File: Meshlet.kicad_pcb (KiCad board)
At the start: 2 copper layers, 60.2 x 39 mm, 114 parts, among them J1 Ext. Notif. Header, J10 STEMMA QT I2C, J11 GPIO Exp., J12 I2C PINHEADER, J13 Ext. Power Header, J2 USB_C_Receptacle_USB2.0_16P, J3 Ext. Power Header, J4 Batt. Header (JST-PH 2.0), J5 SWD, J6 Batt. Header (Picoblade 1.25), J7 GPS Header, J8 User Btn Header, J9 Power Switch, Q1 AO3400A, SW1 BOOTSEL, SW3 RST, U1 W25Q32JVZP, U10 XC6206PxxxMR, U11 XC6206PxxxMR, U2 XC6206PxxxMR, U3 RP2350_60QFN, U4 INA3221, U5 BME280, U6 Wio-SX1262, U7 USBLC6-2SC6, U8 BQ24074RGT, Y1 12.000MHz

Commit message: Redesign!
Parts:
- removed G***: LOGO, Graphics:HalftoneOverlay
- removed J10: STEMMA QT I2C, Connector_JST:JST_PH_S4B-PH-SM4-TB_1x04-1MP_P2.00mm_Horizontal
- removed J8: User Btn Header, Connector_PinHeader_1.27mm:PinHeader_1x02_P1.27mm_Vertical
- removed JP6: PwrSw Bypass, Jumper:SolderJumper-2_P1.3mm_Bridged_RoundedPad1.0x1.5mm
- removed R29, R30, R33, R34, R35: 10k, Resistor_SMD:R_0402_1005Metric
- removed R31: 1k, Resistor_SMD:R_0402_1005Metric
- removed R32: 470R, Resistor_SMD:R_0402_1005Metric
- removed REF** (x2): MountingHole_2.2mm_M2_Pad_TopBottom, MountingHole:MountingHole_2.2mm_M2_Pad_TopBottom
- removed REF** (x2): ToolingHole_1.152mm, MountingHole:ToolingHole_1.152mm
- removed SW3: RST, Button_Switch_SMD:SW_Push_1P1T_XKB_TS-1187A
- removed TH1: Thermistor_NTC, Resistor_SMD:R_0402_1005Metric_Pad0.72x0.64mm_HandSolder
- added C32: 47uF, Capacitor_SMD:C_0805_2012Metric, B.Cu at (135.9, 109.1)
- added J14: Ext. Notif. Header, Connector_PinHeader_2.00mm:PinHeader_1x02_P2.00mm_Vertical, F.Cu at (123.8, 97.9)
- added JP1: TS, Jumper:SolderJumper-2_P1.3mm_Bridged_RoundedPad1.0x1.5mm, F.Cu at (140.1, 106.8)
- added R5: 27R, Resistor_SMD:R_0402_1005Metric, F.Cu at (145.5, 87.5)
- added SW2: BOOTSEL, Button_Switch_SMD:SW_Push_1P1T_XKB_TS-1187A, F.Cu at (139.1, 96.7)
- C1: value 15pF -> 100nF
- C13, C18, C19: value 100nF -> 1uF
- C14: value 100nF -> 4.7uF
- C15, C17: value 100nF -> 4.7uF; footprint Capacitor_SMD:C_0402_1005Metric -> RP2350 Components:C_0402_1005Metric_small_pads
- C2: value 15pF -> 4.7uF
- C20: value 100nF -> 47uF; footprint Capacitor_SMD:C_0402_1005Metric -> Capacitor_SMD:C_0805_2012Metric
- C21: value 100nF -> 15pF
- C24: value 47uF -> 15pF; footprint Capacitor_SMD:C_0805_2012Metric -> Capacitor_SMD:C_0402_1005Metric
- C25, C9: value 1uF -> 100nF
- C26, C27, C28: value 1uF -> 22uF
- C29, C30: value 47uF -> 1uF; footprint Capacitor_SMD:C_0805_2012Metric -> Capacitor_SMD:C_0402_1005Metric
- C3, C5: value 4.7uF -> 100nF; footprint RP2350 Components:C_0402_1005Metric_small_pads -> Capacitor_SMD:C_0402_1005Metric
- C31: value 47uF -> 100nF; footprint Capacitor_SMD:C_0805_2012Metric -> Capacitor_SMD:C_0402_1005Metric
- C6, C7: value 4.7uF -> 100nF
- D3: value PG -> HB
- D4: value CHG -> PV
- D5: value PWR -> CHG
- D6: value HB -> FLT
- J1: value Ext. Notif. Header -> SWD; footprint Connector_PinHeader_1.27mm:PinHeader_1x02_P1.27mm_Vertical -> Connector_PinHeader_1.27mm:PinHeader_1x03_P1.27mm_Vertical; moved to B.Cu
- J11: footprint Connector_PinHeader_1.27mm:PinHeader_1x04_P1.27mm_Vertical -> Connector_PinHeader_2.00mm:PinHeader_1x05_P2.00mm_Vertical; moved to B.Cu
- J12: value I2C PINHEADER -> GPS Header; footprint Connector_PinHeader_1.27mm:PinHeader_1x04_P1.27mm_Vertical -> Connector_PinHeader_2.00mm:PinHeader_1x05_P2.00mm_Vertical; moved to B.Cu
- J13: value Ext. Power Header -> Thermistor Pins
- J2: value USB_C_Receptacle_USB2.0_16P -> User Btn Header; footprint Connector_USB:USB_C_Receptacle_G-Switch_GT-USB-7010ASV -> Connector_PinHeader_2.00mm:PinHeader_1x02_P2.00mm_Vertical
- J3: value Ext. Power Header -> Batt. Header (Picoblade 1.25); footprint Connector_JST:JST_XH_S2B-XH-A_1x02_P2.50mm_Horizontal -> Connector_Molex:Molex_PicoBlade_53261-0271_1x02-1MP_P1.25mm_Horizontal; moved to B.Cu
- J4: moved to B.Cu
- J5: value SWD -> USB_C_Receptacle_USB2.0_16P; footprint Connector_JST:JST_SH_SM03B-SRSS-TB_1x03-1MP_P1.00mm_Horizontal -> Connector_USB:USB_C_Receptacle_G-Switch_GT-USB-7010ASV
- J6: value Batt. Header (Picoblade 1.25) -> STEMMA QT I2C; footprint Connector_Molex:Molex_PicoBlade_53261-0271_1x02-1MP_P1.25mm_Horizontal -> Connector_PinHeader_2.00mm:PinHeader_1x04_P2.00mm_Vertical; moved to B.Cu
- J7: value GPS Header -> Ext. Power Header; footprint Connector_PinHeader_1.27mm:PinHeader_1x05_P1.27mm_Vertical -> Connector_JST:JST_PH_S2B-PH-SM4-TB_1x02-1MP_P2.00mm_Horizontal
- J9: value Power Switch -> Ext. Power Header; footprint Connector_PinHeader_2.00mm:PinHeader_1x02_P2.00mm_Vertical -> Connector_PinHeader_2.54mm:PinHeader_1x02_P2.54mm_Vertical; moved to B.Cu
- JP2: value ISET -> Chemistry Select; moved to B.Cu
- JP3: value EN1 -> SolderJumper_2_Open; footprint Jumper:SolderJumper-3_P1.3mm_Bridged12_RoundedPad1.0x1.5mm -> Jumper:SolderJumper-2_P1.3mm_Open_RoundedPad1.0x1.5mm
- JP4: value EN2 -> SolderJumper_2_Bridged; footprint Jumper:SolderJumper-3_P1.3mm_Bridged12_RoundedPad1.0x1.5mm -> Jumper:SolderJumper-2_P1.3mm_Bridged_RoundedPad1.0x1.5mm
- JP5: value Jumper_3_Bridged12 -> SolderJumper_2_Open; footprint Jumper:SolderJumper-3_P1.3mm_Bridged12_RoundedPad1.0x1.5mm -> Jumper:SolderJumper-2_P1.3mm_Open_RoundedPad1.0x1.5mm
- R10, R9: value 27R -> 1k
- R16: value 10k -> 13k
- R17: value 10k -> 1k
- R18: value 4.7k -> 5.1k
- R19: value 5.1k -> 300
- R2: value 1k -> 5.1k
- R20: value 5.1k -> 600
- R21: value 4.7k -> 1.2k
- R23, R26: value 1k -> PA2512FKF7W0R01E; footprint Resistor_SMD:R_0402_1005Metric -> Resistor_SMD:R_2512_6332Metric
- R24: value 10k -> PA2512FKF7W0R01E; footprint Resistor_SMD:R_0402_1005Metric -> Resistor_SMD:R_2512_6332Metric
- R25: value 10k -> 470R
- R27: value 1k -> 10k
- R3: value 0 -> 5.1k
- R4: value 1k -> 27R
- R6, R7, R8: value PA2512FKF7W0R01E -> 10k; footprint Resistor_SMD:R_2512_6332Metric -> Resistor_SMD:R_0402_1005Metric
- SW1: value BOOTSEL -> RST
- U1: value W25Q32JVZP -> XC6206PxxxMR; footprint Package_SON:WSON-8-1EP_6x5mm_P1.27mm_EP3.4x4.3mm -> Package_TO_SOT_SMD:SOT-23-3
- U10: value XC6206PxxxMR -> ~; footprint Package_TO_SOT_SMD:SOT-23-3 -> RM2:Radio Module 2; moved to B.Cu
- U11: value XC6206PxxxMR -> INA3221; footprint Package_TO_SOT_SMD:SOT-23-3 -> Package_DFN_QFN:Texas_RGV0016A_VQFN-16-1EP_4x4mm_P0.65mm_EP2.1x2.1mm
- U2: value XC6206PxxxMR -> USBLC6-2SC6; footprint Package_TO_SOT_SMD:SOT-23-3 -> Package_TO_SOT_SMD:SOT-23-6
- U3: value RP2350_60QFN -> XC6206PxxxMR; footprint RP2350_60QFN_minimal:RP2350-QFN-60-1EP_7x7_P0.4mm_EP3.4x3.4mm_ThermalVias -> Package_TO_SOT_SMD:SOT-23-3
- U4: value INA3221 -> RP2350_60QFN; footprint Package_DFN_QFN:Texas_RGV0016A_VQFN-16-1EP_4x4mm_P0.65mm_EP2.1x2.1mm -> RP2350_60QFN_minimal:RP2350-QFN-60-1EP_7x7_P0.4mm_EP3.4x3.4mm_ThermalVias
- U5: value BME280 -> Wio-SX1262; footprint Package_LGA:Bosch_LGA-8_2.5x2.5mm_P0.65mm_ClockwisePinNumbering -> Wio-SX1262:Wio-SX1262; moved to B.Cu
- U6: value Wio-SX1262 -> BQ25185; footprint Wio-SX1262:Wio-SX1262 -> Package_DFN_QFN:Texas_DLH0010A_WSON-10-1EP_2.2x2mm_P0.4mm_EP0.9x1.5mm_ThermalVias
- U7: value USBLC6-2SC6 -> BME280; footprint Package_TO_SOT_SMD:SOT-23-6 -> Package_LGA:Bosch_LGA-8_2.5x2.5mm_P0.65mm_ClockwisePinNumbering
- U8: value BQ24074RGT -> W25Q32JVZP; footprint Package_DFN_QFN:VQFN-16-1EP_3x3mm_P0.5mm_EP1.6x1.6mm -> Package_SON:WSON-8-1EP_6x5mm_P1.27mm_EP3.4x4.3mm
- U9: value ~ -> XC6206PxxxMR; footprint RM2:Radio Module 2 -> Package_TO_SOT_SMD:SOT-23-3; moved to F.Cu
- moved J7 58.9 mm to (160.2, 97.9)
- moved U9 57.4 mm to (134.1, 102.6)
- moved J5 49.3 mm to (161.2, 87.7), turned to 90 degrees
- moved F3 47.7 mm to (131.7, 103.0)
- moved J13 47.0 mm to (142.4, 103.3), turned to 90 degrees
- moved R21 46.7 mm to (132.6, 108.9), turned to 180 degrees
- moved R19 45.3 mm to (137.6, 108.9), turned to 180 degrees
- moved R20 44.8 mm to (135.1, 108.9), turned to 180 degrees
- moved C27 44.5 mm to (154.2, 106.6)
- moved C28 43.9 mm to (150.7, 107.9), turned to 180 degrees
- moved U6 43.0 mm to (153.3, 108.3), turned to 0 degrees
- moved U5 42.3 mm to (122.8, 80.3), turned to 0 degrees
- moved R2 41.3 mm to (157.2, 81.0), turned to 180 degrees
- moved R3 40.8 mm to (157.2, 82.0), turned to 0 degrees
- moved SW1 39.9 mm to (131.6, 96.7), turned to 0 degrees
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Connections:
- C1 pad 1: GND -> +1V1
- C1 pad 2: XIN -> GND
- C12 pad 1: /Pi +3V3 -> Net-(U1-VI)
- C13 pad 1: /Pi +3V3 -> +3V3
- C14 pad 1: /Pi +3V3 -> Net-(U4-VREG_AVDD)
- C16 pad 1: /Pi +3V3 -> USB_RAW
- C17 pad 1: GND -> +1V1
- C17 pad 2: +3V3 -> GND
- C18 pad 1: /Pi +3V3 -> Net-(U3-VI)
- C19 pad 1: /Pi +3V3 -> /LoRa +3V3
- C2 pad 1: GND -> +1V1
- C2 pad 2: Net-(C2-Pad2) -> GND
- C20 pad 1: /Pi +3V3 -> GND
- C20 pad 2: GND -> /LoRa +3V3
- C21 pad 1: +3V3 -> GND
- C21 pad 2: GND -> XIN
- C23 pad 1: INA_IN3- -> +3V3
- C24 pad 2: BMS_OUT -> Net-(C24-Pad2)
- C25 pad 1: Net-(U10-VI) -> /Pi +3V3
- C26 pad 1: /LoRa +3V3 -> BMS_INA
- C27 pad 1: Net-(U11-VI) -> VBUS_OUT
- C28 pad 1: +3V3 -> BATT
- C29 pad 1: BMS_OUT -> Net-(U9-VI)
- C3 pad 1: /Pi +3V3 -> +1V1
- C30 pad 1: INA_IN1+ -> /Pi +3V3
- C31 pad 2: /LoRa +3V3 -> +3V3
- C4 pad 1: +1V1 -> /Pi +3V3
- C5 pad 1: +1V1 -> /Pi +3V3
- C6 pad 1: Net-(U3-VREG_AVDD) -> /Pi +3V3
- C7 pad 1: +1V1 -> /Pi +3V3
- C8 pad 1: +1V1 -> /Pi +3V3
- C9 pad 1: Net-(U2-VI) -> /Pi +3V3
- D1 pad 1: VBUS -> VBUS_INA
- D1 pad 2: INA_IN3+ -> USB_RAW
- D2 pad 1: VBUS -> VBUS_INA
- D2 pad 2: INA_IN2+ -> Net-(D2-A)
- D3 pad 1: Net-(D3-K) -> GND
- D3 pad 2: BMS_OUT -> Net-(D3-A)
- D6 pad 1: GND -> Net-(D6-K)
- D6 pad 2: Net-(D6-A) -> BMS_OUT
- F1 pad 2: Net-(U2-VI) -> Net-(U1-VI)
- F2 pad 2: Net-(U10-VI) -> Net-(U3-VI)
- F3 pad 2: Net-(U11-VI) -> Net-(U9-VI)
- J1 pad 1: +3V3 -> SWCLK
- J1 pad 2: Net-(J1-Pin_2) -> GND
- J11 pad 1: +3V3 -> GP4
- J11 pad 2: INA_IN3- -> GP16
- J11 pad 3: BMS_OUT -> GP18
- J11 pad 4: GND -> GP19
- J12 pad 3: I2C_SCL -> GPS_TX
- J12 pad 4: I2C_SDA -> GPS_RX
- J13 pad 1: GND -> THERM
- J13 pad 2: INA_IN2- -> GND
- J3 pad 2: INA_IN2- -> BATT_INA
- J4 pad 2: INA_IN1- -> BATT_INA
- J6 pad 1: INA_IN1- -> I2C_SDA
- J6 pad 2: GND -> I2C_SCL
- J7 pad 2: +3V3 -> Net-(D2-A)
- J9 pad 1: Net-(J9-Pin_1) -> GND
- J9 pad 2: BMS_OUT -> Net-(D2-A)
- JP3 pad 1: BMS_OUT -> Net-(JP3-A)
- JP3 pad 2: BMS_EN1 -> ISET
- JP4 pad 1: GND -> Net-(JP4-A)
- JP4 pad 2: BMS_EN2 -> ISET
- JP5 pad 2: Net-(JP5-C) -> ISET
- L1 pad 2: Net-(U3-VREG_LX) -> Net-(U4-VREG_LX)
- Q1 pad 3: Net-(J1-Pin_2) -> Net-(J14-Pin_2)
- R1 pad 2: Net-(U3-VREG_AVDD) -> Net-(U4-VREG_AVDD)
- R10 pad 1: USB_DN -> Net-(R10-Pad1)
- R10 pad 2: Net-(U3-USB_DM) -> QSPI_SS
- R11 pad 1: INA_VPU -> Net-(U6-STAT1)
- R11 pad 2: INA_PV -> Net-(D6-K)
- R12 pad 1: +3V3 -> Net-(U6-STAT2)
- R12 pad 2: INA_CRIT -> Net-(D5-K)
- R13 pad 1: +3V3 -> GND
- R13 pad 2: INA_WARN -> Net-(U6-CE)
- R14 pad 1: +3V3 -> Net-(JP1-B)
- R14 pad 2: INA_TC -> GND
- R15 pad 1: +3V3 -> Net-(D4-K)
- R15 pad 2: I2C_SCL -> GND
- R16 pad 1: +3V3 -> VSET
- R16 pad 2: I2C_SDA -> Net-(JP2-B)
- R17 pad 1: NOTIFY -> Net-(C24-Pad2)
- R17 pad 2: Net-(Q1-G) -> XOUT
- R18 pad 1: I2C_SDA -> Net-(JP2-A)
- R18 pad 2: +3V3 -> VSET
- R19 pad 1: Net-(J2-CC1) -> GND
- R19 pad 2: GND -> Net-(JP3-A)
- R2 pad 1: Net-(R2-Pad1) -> Net-(J5-CC1)
- R2 pad 2: QSPI_SS -> GND
- R20 pad 2: Net-(J2-CC2) -> Net-(JP4-A)
- R21 pad 1: I2C_SCL -> GND
- R21 pad 2: +3V3 -> Net-(JP5-A)
- R22 pad 1: Net-(U8-ISET) -> INA_VPU
- R22 pad 2: Net-(JP2-A) -> INA_PV
- R23 pad 1: Net-(U8-ISET) -> BATT
- R23 pad 2: Net-(JP2-B) -> BATT_INA
- R24 pad 1: GND -> VBUS_INA
- R24 pad 2: Net-(U8-ITERM) -> VBUS_OUT
- R25 pad 1: Net-(U8-~{CE}) -> GP24
- R25 pad 2: GND -> Net-(U10-DO)
- R26 pad 1: GND -> BMS_INA
- R26 pad 2: Net-(U8-ILIM) -> BMS_OUT
- R27 pad 1: USER_BTN -> NOTIFY
- R27 pad 2: GND -> Net-(Q1-G)
- R28 pad 1: Net-(U8-~{PGOOD}) -> GP24
- R28 pad 2: Net-(D3-K) -> Net-(U10-IRQ)
- R3 pad 1: Net-(U1-~{CS}) -> GND
- R3 pad 2: QSPI_SS -> Net-(J5-CC2)
- R4 pad 1: Net-(C2-Pad2) -> USB_DP
- R4 pad 2: XOUT -> Net-(U4-USB_DP)
- R6 pad 1: INA_IN1+ -> +3V3
- R6 pad 2: INA_IN1- -> I2C_SCL
- R7 pad 1: INA_IN2+ -> +3V3
- R7 pad 2: INA_IN2- -> I2C_SDA
- R8 pad 1: INA_IN3+ -> Net-(D3-A)
- R8 pad 2: INA_IN3- -> Net-(U4-GPIO14)
- R9 pad 1: USB_DP -> Net-(R9-Pad1)
- R9 pad 2: Net-(U3-USB_DP) -> GND
- SW1 pad 1: Net-(R2-Pad1) -> Net-(U4-RUN)
- SW1 pad 2: GND -> Net-(R9-Pad1)
- U1 pad 1: Net-(U1-~{CS}) -> GND
- U1 pad 2: QSPI_SD1 -> +3V3
- U1 pad 3: QSPI_SD2 -> Net-(U1-VI)
- U10 pad 2: /LoRa +3V3 -> unconnected-(U10-NC-Pad2)
- U10 pad 3: Net-(U10-VI) -> GP29
- U11 pad 1: GND -> BMS_OUT
- U11 pad 2: +3V3 -> BMS_INA
- U11 pad 3: Net-(U11-VI) -> GND
- U2 pad 1: GND -> USB_DP
- U2 pad 2: /Pi +3V3 -> GND
- U2 pad 3: Net-(U2-VI) -> USB_DN
- U3 pad 1: /Pi +3V3 -> GND
- U3 pad 2: GPS_RX -> /LoRa +3V3
- U3 pad 3: GPS_TX -> Net-(U3-VI)
- U4 pad 1: INA_IN3- -> /Pi +3V3
- U4 pad 10: INA_PV -> unconnected-(U4-GPIO7-Pad10)
- U4 pad 11: INA_IN1- -> /Pi +3V3
- U4 pad 12: INA_IN1+ -> I2C_SDA
- U4 pad 13: INA_TC -> I2C_SCL
- U4 pad 14: INA_IN2- -> LORA_SCK
- U4 pad 15: INA_IN2+ -> LORA_MOSI
- U4 pad 16: INA_VPU -> LORA_MISO
- U4 pad 17: GND -> LORA_RF_SW
- U4 pad 2: INA_IN3+ -> GPS_RX
- U4 pad 3: GND -> GPS_TX
- U4 pad 4: +3V3 -> LORA_BUSY
- U4 pad 5: I2C_SDA -> LORA_CS
- U4 pad 6: I2C_SCL -> +1V1
- U4 pad 7: I2C_SDA -> GPS_EN
- U4 pad 8: INA_WARN -> GP4
- U4 pad 9: INA_CRIT -> unconnected-(U4-GPIO6-Pad9)
- U5 pad 1: GND -> LORA_RF_SW
- U5 pad 2: +3V3 -> LORA_MISO
- U5 pad 3: I2C_SDA -> LORA_MOSI
- U5 pad 4: I2C_SCL -> LORA_SCK
- U5 pad 5: GND -> LORA_RST
- U5 pad 6: +3V3 -> LORA_CS
- U5 pad 8: +3V3 -> /LoRa +3V3
- U6 pad 1: LORA_RF_SW -> BMS_INA
- U6 pad 10: GND -> VBUS_OUT
- U6 pad 11: LORA_BUSY -> GND
- U6 pad 2: LORA_MISO -> BATT
- U6 pad 3: LORA_MOSI -> Net-(U6-STAT2)
- U6 pad 4: LORA_SCK -> Net-(U6-CE)
- U6 pad 5: LORA_RST -> GND
- U6 pad 6: LORA_CS -> THERM
- U6 pad 7: GND -> VSET
- U6 pad 8: /LoRa +3V3 -> ISET
- U6 pad 9: unconnected-(U6-ANT-Pad9) -> Net-(U6-STAT1)
- U7 pad 1: USB_DP -> GND
- U7 pad 2: GND -> +3V3
- U7 pad 3: USB_DN -> I2C_SDA
- U7 pad 4: USB D- -> I2C_SCL
- U7 pad 5: INA_IN3- -> GND
- U7 pad 6: USB D+ -> +3V3
- U8 pad 1: Net-(JP5-C) -> QSPI_SS
- U8 pad 2: INA_IN1+ -> QSPI_SD1
- U8 pad 3: INA_IN1+ -> QSPI_SD2
- U8 pad 4: Net-(U8-~{CE}) -> GND
- U8 pad 5: BMS_EN2 -> QSPI_SD0
- U8 pad 6: BMS_EN1 -> QSPI_SCLK
- U8 pad 7: Net-(U8-~{PGOOD}) -> QSPI_SD3
- U8 pad 8: GND -> /Pi +3V3
- U8 pad 9: Net-(U8-~{CHG}) -> GND
- U9 pad 2: unconnected-(U9-NC-Pad2) -> /Pi +3V3
- U9 pad 3: GP29 -> Net-(U9-VI)
- Y1 pad 3: Net-(C2-Pad2) -> Net-(C24-Pad2)
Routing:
- net +3V3: track 155.0 -> 76.2 mm
- net I2C_SCL: track 110.2 -> 41.2 mm
- net I2C_SDA: track 109.1 -> 43.3 mm
- net BMS_OUT: track 110.8 -> 51.2 mm, vias 2 -> 4
- net INA_IN3-: track 48.5 -> 0.00 mm, vias 4 -> 0
- net GP29: track 48.1 -> 0.00 mm, vias 1 -> 0
- net GND: track 49.4 -> 1.75 mm, vias 323 -> 4
- net /Pi +3V3: track 99.3 -> 53.8 mm, vias 4 -> 3
- net Net-(U3-RUN): track 44.2 -> 0.00 mm, vias 2 -> 0
- net INA_IN1+: track 40.8 -> 0.00 mm, vias 2 -> 0
- net INA_IN1-: track 35.4 -> 0.00 mm
- net USB_RAW: track 0.00 -> 34.9 mm, vias 0 -> 2
- net INA_IN2-: track 31.4 -> 0.00 mm
- net GP25: track 42.9 -> 11.8 mm
- net Net-(D2-A): track 0.00 -> 30.9 mm, vias 0 -> 2
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- added copper zone on F.Cu, net BATT
- added copper zone on F.Cu, net BMS_INA
- added copper zone on In1.Cu, net GND
- added copper zone on In2.Cu, net GND
- added copper zone on F.Cu, net Net-(U4-VREG_LX)
- added copper zone on F.Cu, net VBUS_OUT
- removed copper zone on F.Cu, net Net-(U3-VREG_LX)
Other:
- board size 60.2 x 39 mm -> 42.5 x 32 mm
- copper layers 2 -> 4
- board text removed: "!"
- board text removed: "*4V4 MAX"
- board text removed: "*BMS"
- board text removed: "+"
- board text removed: "-"
- board text removed: "0"
- board text removed: "0.5A"
- board text removed: "1"
- board text removed: "1 SERIES CELL ONLY!"
- board text removed: "1A"
- board text removed: "3V"
- board text removed: "3V3"
- board text removed: "5V-10V"
- board text removed: ":"
- board text removed: "BOOT"
- board text removed: "Charge Rate (default 0.5A, 1A jumped)"
- board text removed: "DESIGNED IN"
- board text removed: "EDMONTON, AB"
- board text removed: "EN"
- board text removed: "EN1"
- board text removed: "EN1 (see datasheet, default high)"
- board text removed: "EN2"
- board text removed: "EN2 (see datasheet, default low)"
- board text removed: "EP V0.2"
- board text removed: "EXT. DC, SOLAR"
- board text removed: "EXTERNAL NOTIFS"
- board text removed: "GND"
- board text removed: "GP0"
- board text removed: "GP1"
- board text removed: "GP22"
- board text removed: "GP5"
- board text removed: "GPS"
- board text removed: "HEY!"
- board text removed: "I HOPE YOU HAVE A LONG ENOUGH USB CABLE"
- board text removed: "I2C"
- board text removed: "ISET"
- board text removed: "JP1:"
- board text removed: "JP2:"
- board text removed: "JP3:"
- board text removed: "JP4:"
- board text removed: "JP5:"
- board text removed: "JUMPER FUNCTIONS"
- board text removed: "LITHIUM ION & POLYMER"
- board text removed: "M2"
- board text removed: "MESH NETWORK NODE RP2350 MESH NETWORK NODE RP2350"
- board text removed: "MESHLET"
- board text removed: "MULTIPLE CELLS IN PARALLEL ARE OK IF YOU KNOW WHAT YOU'RE DOING"
- board text removed: "NOTIF."
- board text removed: "ON REAR"
- board text removed: "OUTPUTS ONLY! **"
- board text removed: "PINOUT ON REAR"
- board text removed: "PUT ME BACK!"
- board text removed: "PWR OUT"
- board text removed: "PWR SW."
- board text removed: "Pwr Sw. Bypass (cut to add pwr switch)"
- board text removed: "RP2350 MESH NETWORK NODE"
- board text removed: "RPI RM2"
- board text removed: "RST"
- board text removed: "RX"
- board text removed: "SCL"
- board text removed: "SDA"
- board text removed: "STEMMA I2C"
- board text removed: "SWD"
- board text removed: "THE BQ24074 IS A 1-CELL SERIES CHARGER ONLY!"
- board text removed: "TX"
- board text removed: "Thermistor (cut & jump to 1 if present)"
- board text removed: "USB"
- board text removed: "USER BUTTON"
- board text removed: "VERSION 0.2"
- board text removed: "https://5panel.dance/Meshlet"
- board text removed: "×"
- board text removed: "×1"
- board text removed: "↑BATTERY↓"

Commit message: 4 layer ver. complete!
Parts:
- removed J1: SWD, Connector_PinHeader_1.27mm:PinHeader_1x03_P1.27mm_Vertical
- removed J11: GPIO Exp., Connector_PinHeader_2.00mm:PinHeader_1x05_P2.00mm_Vertical
- removed J12: GPS Header, Connector_PinHeader_2.00mm:PinHeader_1x05_P2.00mm_Vertical
- removed R9: 1k, Resistor_SMD:R_0402_1005Metric
- removed SW1: RST, Button_Switch_SMD:SW_Push_1P1T_XKB_TS-1187A
- C32: moved to F.Cu
- moved JP5 7.88 mm to (124.7, 107.0)
- moved R21 7.88 mm to (124.7, 109.1)
- moved JP4 7.24 mm to (127.8, 107.0)
- moved R20 7.24 mm to (127.8, 109.1)
- moved JP3 6.61 mm to (131.0, 107.0)
- moved R19 6.61 mm to (131.0, 109.1)
- moved JP1 5.97 mm to (134.1, 107.0)
- moved R14 5.97 mm to (134.1, 109.1)
- moved D4 2.43 mm to (140.1, 107.0)
- moved R15 2.43 mm to (140.1, 109.2)
- moved C32 2.12 mm to (136.4, 107.0)
- moved J6 2.00 mm to (152.8, 79.8)
- moved R18 1.74 mm to (161.0, 109.6)
- moved JP2 1.74 mm to (161.9, 107.9)
- moved R16 1.74 mm to (162.8, 109.6)
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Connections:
- J6 pad 1: I2C_SDA -> I2C_SCL
- J6 pad 2: I2C_SCL -> I2C_SDA
- R6 pad 1: +3V3 -> /Pi +3V3
- R7 pad 1: +3V3 -> /Pi +3V3
- R8 pad 2: Net-(U4-GPIO14) -> HB
- U4 pad 10: unconnected-(U4-GPIO7-Pad10) -> HB
- U4 pad 18: Net-(U4-GPIO14) -> unconnected-(U4-GPIO14-Pad18)
- U4 pad 26: Net-(U4-RUN) -> /Pi +3V3
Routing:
- net /Pi +3V3: track 53.8 -> 102.9 mm, vias 3 -> 8
- net GP29: track 0.00 -> 36.4 mm, vias 0 -> 1
- net HB: track 0.00 -> 28.4 mm
- net I2C_SDA: track 43.3 -> 54.6 mm
- net Net-(U4-RUN): track 11.1 -> 0.00 mm, vias 2 -> 0
- net ISET: track 28.6 -> 37.3 mm
- net I2C_SCL: track 41.2 -> 47.9 mm
- net THERM: track 22.7 -> 29.1 mm, vias 1 -> 0
- net BMS_OUT: track 51.2 -> 45.8 mm, vias 4 -> 9
- net INA_VPU: track 14.9 -> 10.1 mm
- net +3V3: track 76.2 -> 71.7 mm, vias 4 -> 5
- net SWCLK: track 4.35 -> 0.00 mm, vias 1 -> 0
- net SWDIO: track 3.81 -> 0.00 mm, vias 1 -> 0
- net VBUS_OUT: track 29.2 -> 26.7 mm
- net GP18: track 2.30 -> 0.00 mm
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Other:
- outline, holes or cut-outs redrawn
- board text added: "1000"
- board text added: "250"
- board text added: "500"
- board text added: "CHARGE RATE"
- board text added: "CHEM"
- board text added: "CUT NTC PAD"
- board text added: "LiFePO4"
- board text added: "LiPo"
- board text added: "NTC"
- board text added: "mA"
- board text added: "oh"
- board text added: "uh"

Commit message: Graphics!
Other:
- board text added: ":"
- board text added: "HEY!"
- board text added: "I HOPE YOU HAVE A LONG ENOUGH USB CABLE"
- board text added: "MESHLET"
- board text added: "PUT ME BACK!"
- board text added: "RP2350 MESH NETWORK NODE RP2350 MESH NETWORK NODE"
- board text added: "RPI RM2"
- board text added: "V2"

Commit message: Small changes
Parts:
- moved J9 0.63 mm to (162.9, 85.5)
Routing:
- net GND: vias 336 -> 323
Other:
- board text added: "NETWORK NODE RP2350 MESH NETWORK NODE RP2350 MESH NETWORK NODE"
- board text removed: "RP2350 MESH NETWORK NODE RP2350 MESH NETWORK NODE"

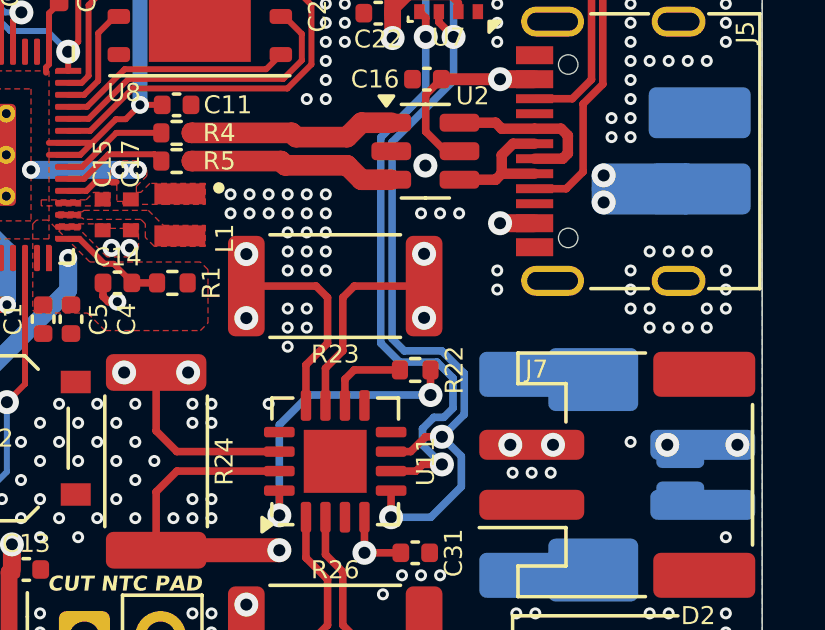
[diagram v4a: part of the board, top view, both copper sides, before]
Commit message: silkscreen tweaks
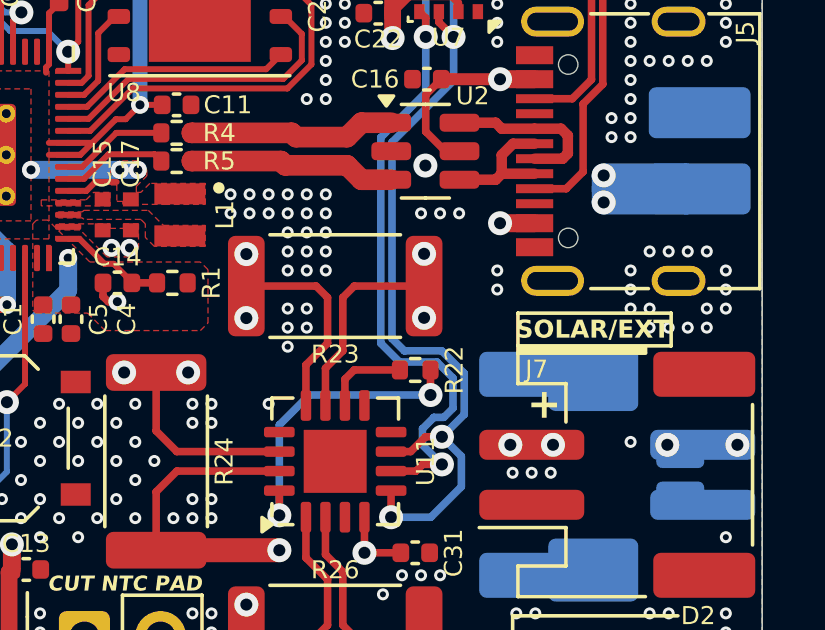
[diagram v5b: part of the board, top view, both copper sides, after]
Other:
- board text added: "+"
- board text added: "DESIGNED IN EDMONTON, AB"
- board text added: "SOLAR/EXT"
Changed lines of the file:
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@@
 		(descr "Inductor with Polarity Marking 2016")
 		(property "Reference" "L1"
-			(at 0.783602 -1.49701 90)
+			(at -0.002201 -1.503101 90)
 			(layer "F.SilkS")
 			(effects
@@
 		(layer "F.SilkS")
 	)
+	(gr_rect
+		(start 156.8068 92.1978)
+		(end 161.9122 93.29)
+		(stroke
+			(width 0.12)
+			(type solid)
+		)
+		(fill no)
+		(layer "F.SilkS")
+	)
 	(gr_poly
 		(pts
@@
 		(layer "F.SilkS")
 	)
+	(gr_rect
+		(start 156.8068 93.299101)
+		(end 161.0614 93.526799)
+		(stroke
+			(width 0.12)
+			(type solid)
+		)
+		(fill yes)
+		(layer "F.SilkS")
+	)
 	(gr_line
 		(start 138.4173 106.903992)
@@
 		)
 	)
+	(gr_text "+"
+		(at 157.6832 95.2246 0)
+		(layer "F.SilkS")
+		(effects
+			(font
+				(size 1 1)
+				(thickness 0.2)
+				(bold yes)
+			)
+		)
+	)
 	(gr_text "uh"
 		(at 144.5133 107.044 0)
@@
 		)
 	)
+	(gr_text "SOLAR/EXT"
+		(at 156.7306 93.0868 0)
+		(layer "F.SilkS" knockout)
+		(effects
+			(font
+				(size 0.6 0.6)
+				(thickness 0.15)
+				(bold yes)
+			)
+			(justify left bottom)
+		)
+	)
 	(gr_text "oh"
 		(at 144.510564 108.0572 0)
@@
 		)
 	)
+	(gr_text "DESIGNED IN EDMONTON, AB"
+		(at 134.8486 109.728 270)
+		(layer "B.SilkS")
+		(effects
+			(font
+				(size 0.6 0.6)
+				(thickness 0.15)
+				(bold yes)
+				(italic yes)
+			)
+			(justify left bottom mirror)
+		)
+	)
 	(gr_text ":"
 		(at 125.2855 107.9627 270)
@@
 	)
 	(group ""
+		(members "164003b1-9e73-4dda-be4f-50f63a7173fb" "f9a48b65-554e-46d3-976c-d6a0db843fb6")
+	)
+	(group ""

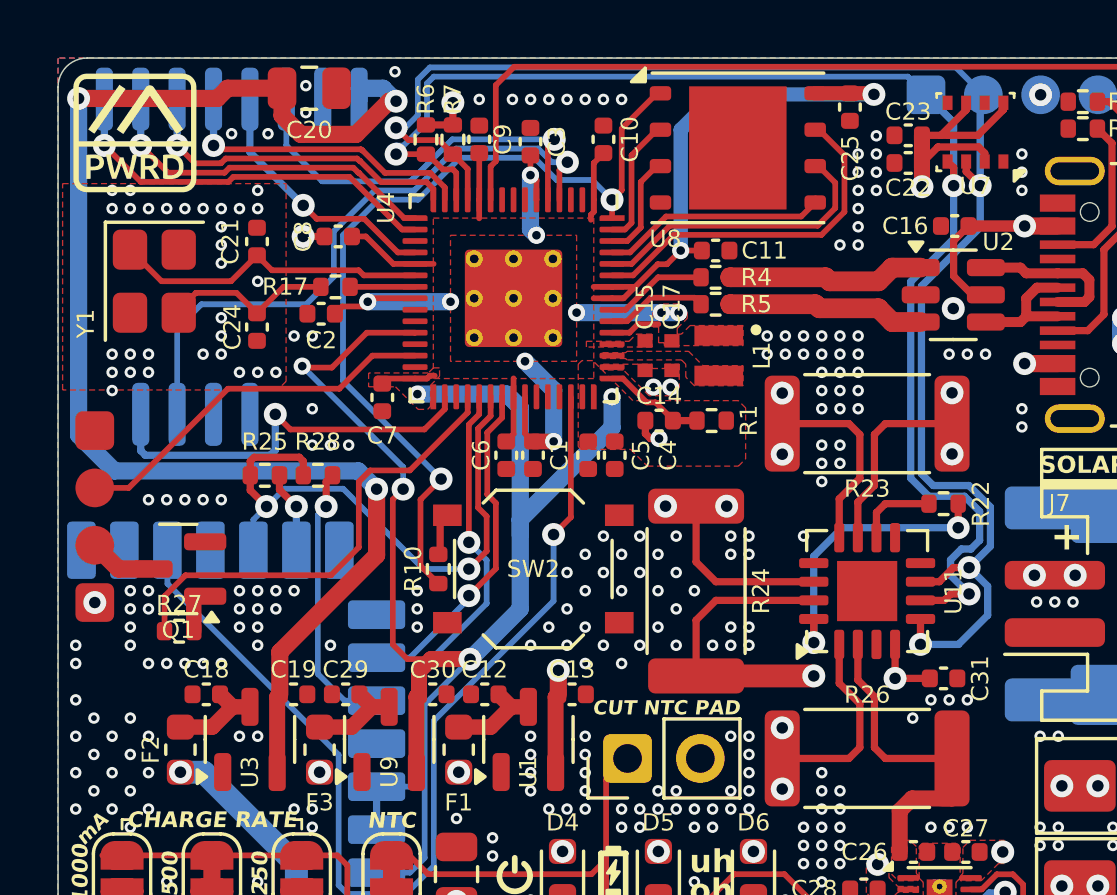
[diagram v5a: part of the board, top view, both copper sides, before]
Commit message: Silkscreen tweaks, update docs
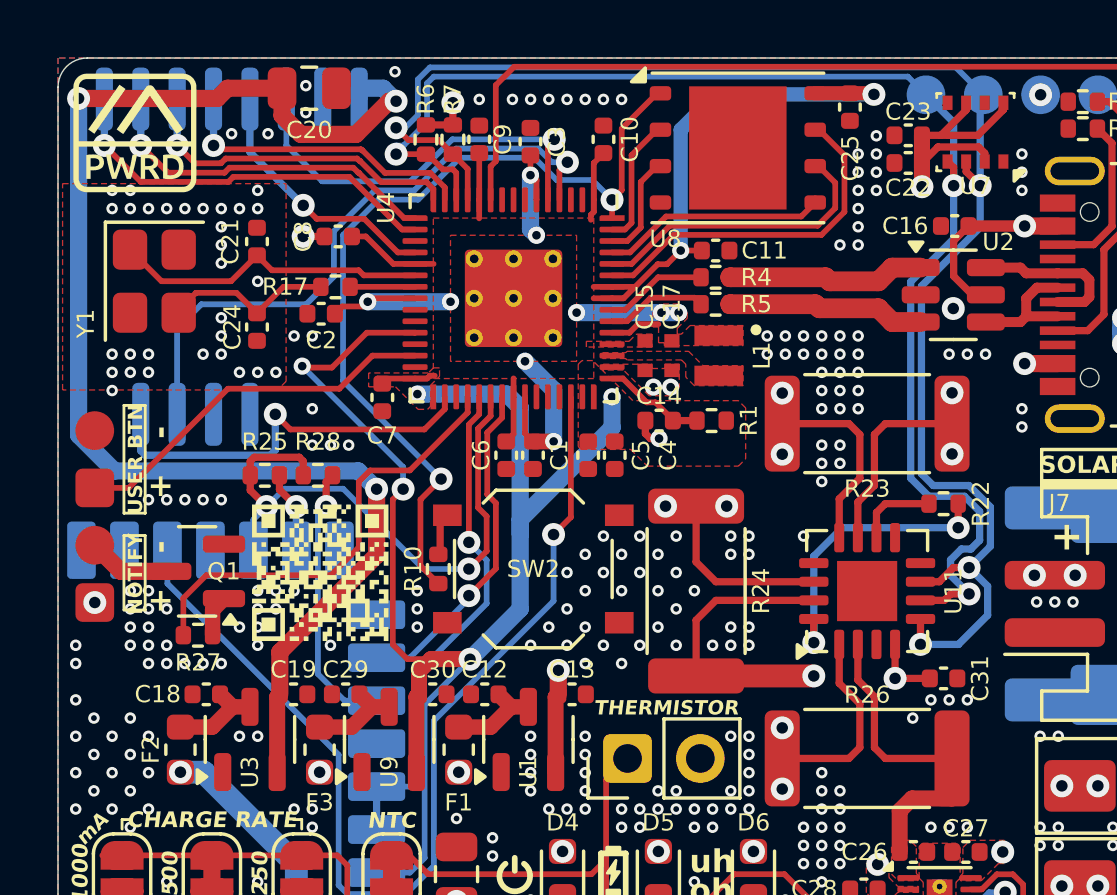
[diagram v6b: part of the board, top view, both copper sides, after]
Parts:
- moved R27 0.67 mm to (127.4, 98.7)
- moved Q1 0.66 mm to (127.3, 96.5)
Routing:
- net Net-(J14-Pin_2): track 2.32 -> 3.01 mm
- net NOTIFY: track 16.3 -> 15.8 mm
- net GND: vias 323 -> 325
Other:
- board text added: "-"
- board text added: "3V3"
- board text added: "5panel.dance/Meshlet"
- board text added: "BATTERY"
- board text added: "EXT. INPUT 3.3V-18V"
- board text added: "GND"
- board text added: "NETWORK NODE"
- board text added: "NOTIFY"
- board text added: "RP2350 MESH NETWORK"
- board text added: "RP2350 MESH NETWORK NODE"
- board text added: "SCL"
- board text added: "SDA"
- board text added: "THERMISTOR"
- board text added: "USER BTN"
- board text added: "for instructions, visit"
- board text removed: "CUT NTC PAD"
- board text removed: "MESHLET"
- board text removed: "NETWORK NODE RP2350 MESH NETWORK NODE RP2350 MESH NETWORK NODE"

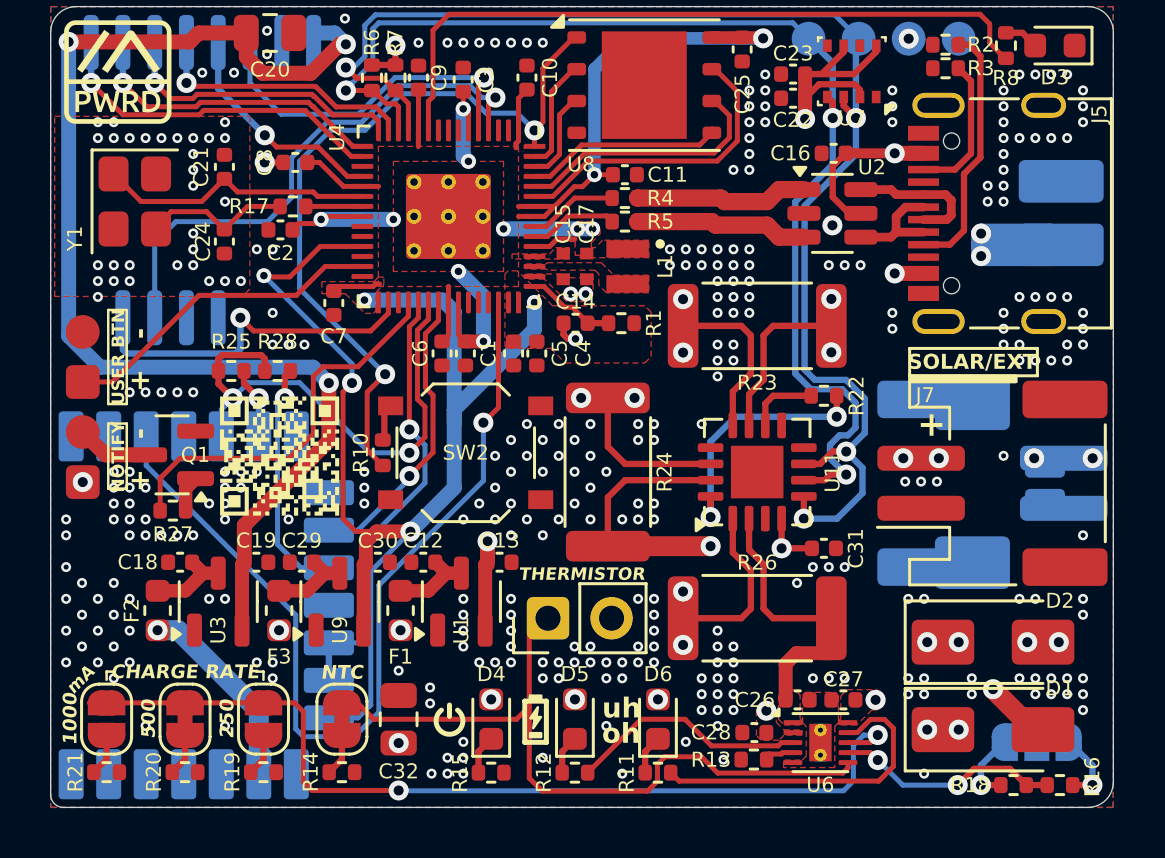
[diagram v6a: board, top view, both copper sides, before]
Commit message: Add interactive BOM
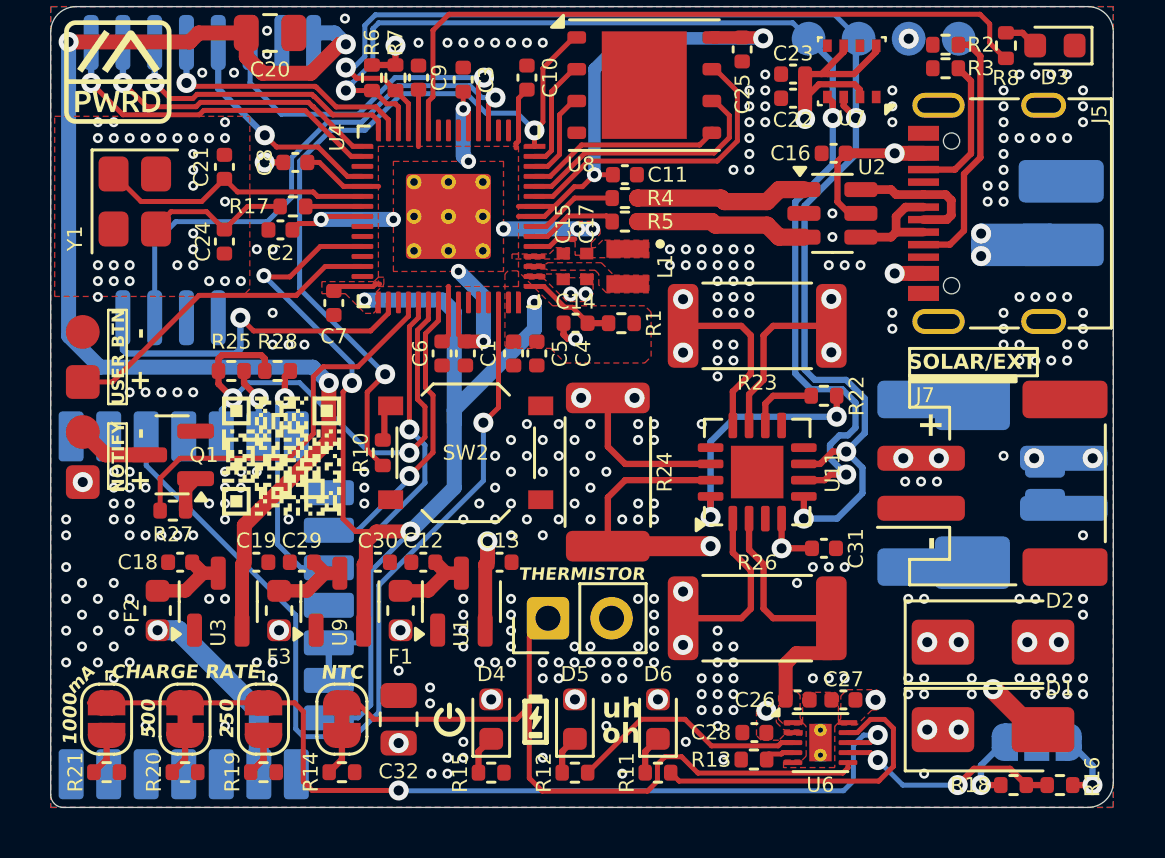
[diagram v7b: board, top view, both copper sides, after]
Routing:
- net GND: vias 325 -> 323
